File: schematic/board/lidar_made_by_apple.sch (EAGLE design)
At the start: 90 parts, among them J1 U.FL-R-SMT-1_10_, J2 U.FL-R-SMT-1_10_

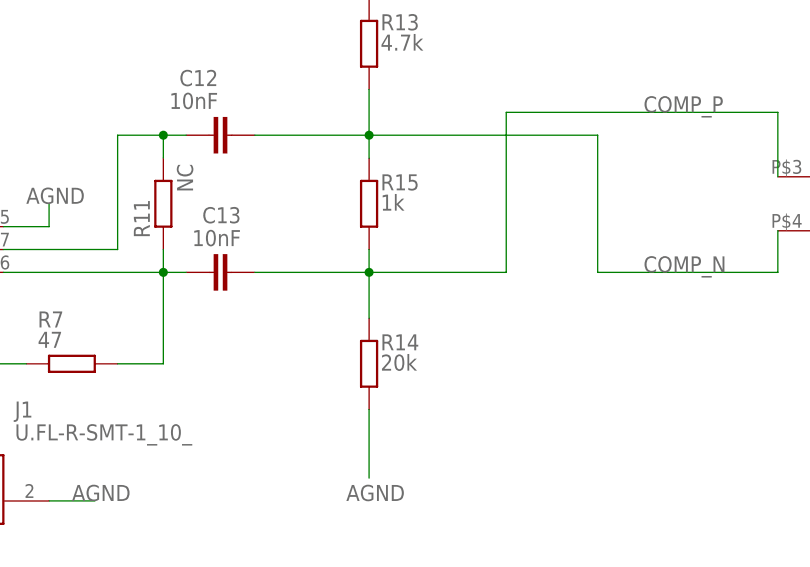
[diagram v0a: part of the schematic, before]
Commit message: передвинул пинхеадер и поменял значения резисторов
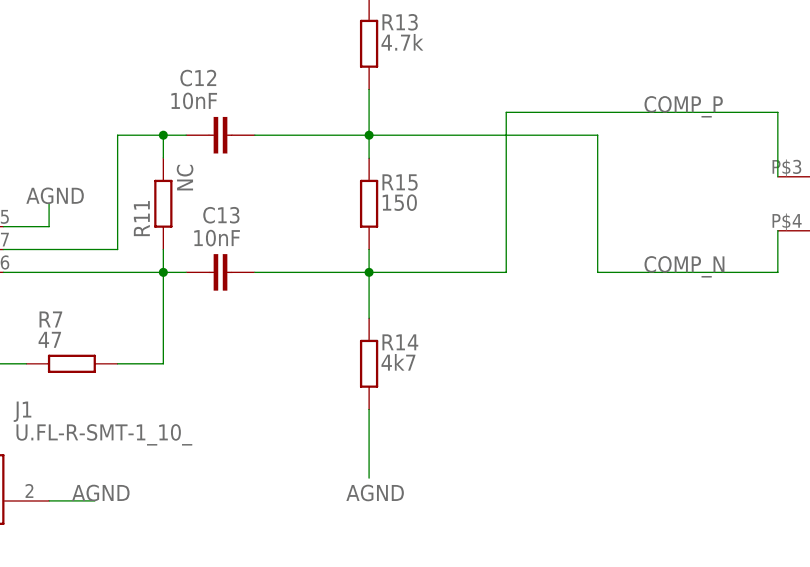
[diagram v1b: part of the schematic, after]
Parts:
- R14: value 20k -> 4k7
- R15: value 1k -> 150
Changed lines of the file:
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@@
 <part name="U$8" library="NEON-BLADE-2024" deviceset="ADCMP600" device=""/>
 <part name="R17" library="rcl" library_urn="urn:adsk.eagle:library:334" deviceset="R-EU_" device="R0603" package3d_urn="urn:adsk.eagle:package:23555/3" value="1k"/>
-<part name="R15" library="rcl" library_urn="urn:adsk.eagle:library:334" deviceset="R-EU_" device="R0603" package3d_urn="urn:adsk.eagle:package:23555/3" value="1k"/>
+<part name="R15" library="rcl" library_urn="urn:adsk.eagle:library:334" deviceset="R-EU_" device="R0603" package3d_urn="urn:adsk.eagle:package:23555/3" value="150"/>
 <part name="R13" library="rcl" library_urn="urn:adsk.eagle:library:334" deviceset="R-EU_" device="R0603" package3d_urn="urn:adsk.eagle:package:23555/3" value="4.7k"/>
-<part name="R14" library="rcl" library_urn="urn:adsk.eagle:library:334" deviceset="R-EU_" device="R0603" package3d_urn="urn:adsk.eagle:package:23555/3" value="20k"/>
+<part name="R14" library="rcl" library_urn="urn:adsk.eagle:library:334" deviceset="R-EU_" device="R0603" package3d_urn="urn:adsk.eagle:package:23555/3" value="4k7"/>
 <part name="C14" library="rcl" library_urn="urn:adsk.eagle:library:334" deviceset="C-EU" device="C0603" package3d_urn="urn:adsk.eagle:package:23616/2" value="1uF"/>
 <part name="R12" library="rcl" library_urn="urn:adsk.eagle:library:334" deviceset="R-EU_" device="R0603" package3d_urn="urn:adsk.eagle:package:23555/3" value="82"/>

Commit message: чёт сделял
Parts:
- removed R12: 82, rcl:R-EU_R0603
- removed R32: NC, rcl:R-EU_R0603
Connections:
- removed net APD_COMP_MCU: R32.2
- removed net N$7: C14.2, R12.1, R13.1
- net 3V3_REF: now also L6.1
- net APD_COMP_OUT: no longer R32.1
- net COMP_DAC: no longer L6.1
- net N$14: now also C14.2, R13.1; no longer R12.2
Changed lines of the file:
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@@
 <part name="R14" library="rcl" library_urn="urn:adsk.eagle:library:334" deviceset="R-EU_" device="R0603" package3d_urn="urn:adsk.eagle:package:23555/3" value="4k7"/>
 <part name="C14" library="rcl" library_urn="urn:adsk.eagle:library:334" deviceset="C-EU" device="C0603" package3d_urn="urn:adsk.eagle:package:23616/2" value="1uF"/>
-<part name="R12" library="rcl" library_urn="urn:adsk.eagle:library:334" deviceset="R-EU_" device="R0603" package3d_urn="urn:adsk.eagle:package:23555/3" value="82"/>
 <part name="C15" library="rcl" library_urn="urn:adsk.eagle:library:334" deviceset="C-EU" device="C0603" package3d_urn="urn:adsk.eagle:package:23616/2" value="100nf"/>
 <part name="J2" library="U.FL-R-SMT-1_10_" deviceset="U.FL-R-SMT-1_10_" device=""/>
@@
 <part name="R27" library="rcl" library_urn="urn:adsk.eagle:library:334" deviceset="R-EU_" device="R0603" package3d_urn="urn:adsk.eagle:package:23555/3" value="0"/>
 <part name="R26" library="rcl" library_urn="urn:adsk.eagle:library:334" deviceset="R-EU_" device="R0603" package3d_urn="urn:adsk.eagle:package:23555/3" value="1k"/>
-<part name="R32" library="rcl" library_urn="urn:adsk.eagle:library:334" deviceset="R-EU_" device="R0603" package3d_urn="urn:adsk.eagle:package:23555/3" value="NC"/>
 <part name="W3" library="NEON-BLADE-2024" deviceset="VIAS-CONNECT" device=""/>
 <part name="U$6" library="NEON-BLADE-2024" deviceset="SPL_PL-90" device=""/>
@@
 <attribute name="VALUE" x="235.204" y="-14.859" size="1.778" layer="96"/>
 </instance>
-<instance part="R12" gate="G$1" x="228.6" y="-7.62" smashed="yes" rot="R90">
-<attribute name="NAME" x="234.95" y="-4.0386" size="1.778" layer="95" rot="R180"/>
-<attribute name="VALUE" x="232.41" y="-6.858" size="1.778" layer="96" rot="R180"/>
-</instance>
 <instance part="C15" gate="G$1" x="279.4" y="-10.16" smashed="yes" rot="R90">
 <attribute name="NAME" x="282.956" y="-15.621" size="1.778" layer="95" rot="R180"/>
@@
 <attribute name="NAME" x="-3.81" y="-110.7186" size="1.778" layer="95" rot="R180"/>
 <attribute name="VALUE" x="-5.842" y="-113.284" size="1.778" layer="96" rot="R180"/>
-</instance>
-<instance part="R32" gate="G$1" x="314.96" y="-53.34" smashed="yes" rot="R270">
-<attribute name="NAME" x="318.9986" y="-49.53" size="1.778" layer="95" rot="R270"/>
-<attribute name="VALUE" x="316.738" y="-49.53" size="1.778" layer="96" rot="R270"/>
 </instance>
 <instance part="W3" gate="G$1" x="76.2" y="-25.4" smashed="yes">
@@
 </segment>
 </net>
-<net name="N$7" class="0">
-<segment>
+<net name="N$14" class="0">
+<segment>
+<pinref part="L6" gate="G$1" pin="2"/>
+<wire x1="228.6" y1="2.54" x2="228.6" y2="-17.78" width="0.1524" layer="91"/>
 <wire x1="228.6" y1="-17.78" x2="233.68" y2="-17.78" width="0.1524" layer="91"/>
-<wire x1="228.6" y1="-17.78" x2="228.6" y2="-12.7" width="0.1524" layer="91"/>
 <pinref part="C14" gate="G$1" pin="2"/>
-<pinref part="R12" gate="G$1" pin="1"/>
 <junction x="228.6" y="-17.78"/>
 <pinref part="R13" gate="G$1" pin="1"/>
@@
 </segment>
 </net>
-<net name="N$14" class="0">
-<segment>
-<pinref part="R12" gate="G$1" pin="2"/>
-<wire x1="228.6" y1="-2.54" x2="228.6" y2="2.54" width="0.1524" layer="91"/>
-<pinref part="L6" gate="G$1" pin="2"/>
-</segment>
-</net>
 <net name="COMP_DAC" class="0">
-<segment>
-<label x="233.68" y="25.4" size="1.778" layer="95" rot="R180"/>
-<pinref part="L6" gate="G$1" pin="1"/>
-<wire x1="228.6" y1="17.78" x2="228.6" y2="22.86" width="0.1524" layer="91"/>
-</segment>
 <segment>
 <pinref part="U$17" gate="G$1" pin="13"/>
@@
 <wire x1="307.34" y1="-43.18" x2="307.34" y2="-45.72" width="0.1524" layer="91"/>
 <wire x1="307.34" y1="-45.72" x2="296.02" y2="-45.72" width="0.1524" layer="91"/>
-<wire x1="307.34" y1="-45.72" x2="314.96" y2="-45.72" width="0.1524" layer="91"/>
 <junction x="307.34" y="-45.72"/>
-<wire x1="325.12" y1="-45.72" x2="314.96" y2="-45.72" width="0.1524" layer="91"/>
-<wire x1="314.96" y1="-45.72" x2="314.96" y2="-48.26" width="0.1524" layer="91"/>
-<junction x="314.96" y="-45.72"/>
-<pinref part="R32" gate="G$1" pin="1"/>
+<wire x1="325.12" y1="-45.72" x2="307.34" y2="-45.72" width="0.1524" layer="91"/>
 <label x="317.5" y="-45.72" size="1.778" layer="95"/>
 </segment>
@@
 <wire x1="177.8" y1="157.48" x2="193.04" y2="157.48" width="0.1524" layer="91"/>
 <label x="180.34" y="157.48" size="1.778" layer="95"/>
-</segment>
-</net>
-<net name="APD_COMP_MCU" class="0">
-<segment>
-<pinref part="R32" gate="G$1" pin="2"/>
-<wire x1="314.96" y1="-58.42" x2="325.12" y2="-58.42" width="0.1524" layer="91"/>
-<label x="320.04" y="-58.42" size="1.778" layer="95"/>
 </segment>
 </net>
@@
 <pinref part="U$4" gate="G$1" pin="VCCI/VCCO"/>
 </segment>
-</net>
+<segment>
+<label x="233.68" y="25.4" size="1.778" layer="95" rot="R180"/>
+<pinref part="L6" gate="G$1" pin="1"/>
+<wire x1="228.6" y1="17.78" x2="228.6" y2="22.86" width="0.1524" layer="91"/>
+</segment>
+</net>

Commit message: опять чёт сделял
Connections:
- removed net COMP_DAC: U$17.13
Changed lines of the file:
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@@
-</segment>
-</net>
-<net name="COMP_DAC" class="0">
-<segment>
-<pinref part="U$17" gate="G$1" pin="13"/>
-<wire x1="195.58" y1="43.18" x2="177.8" y2="43.18" width="0.1524" layer="91"/>
-<label x="177.8" y="43.18" size="1.778" layer="95"/>
 </segment>
 </net>

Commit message: Ошибка повторенная дважды называется - выбор
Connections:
- removed net N$28: C20.1
- net GND: now also C20.1
- net LASER_COMP: no longer U$15.6
- net N$18: now also J2.2
- net PGND: no longer J2.2
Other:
- moved on the sheet: C1, C10, C11, C12, C13, C14, C15, C16, C17, C19, C2, C23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
